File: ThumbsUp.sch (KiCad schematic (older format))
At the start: 169 parts, among them IC1 RP2040, IC2 W25Q128JVSIM, IC3 RP2040, IC4 W25Q128JVSIM, J1 Conn_01x04_Male, J10 Raiser_Male, J11 Raiser_Female, J12 Raiser_Male, J13 Raiser_Female, J14 Raiser_Male, J15 Raiser_Female, J16 Raiser_Male, J17 Raiser_Female, J18 Raiser_Male, J19 Raiser_Female, J2 Conn_01x04_Male, J20 Conn_01x04_Female, J21 Conn_01x04_Female, J22 Conn_01x04_Female, J23 Conn_01x04_Female, J24 Conn_01x04_Male, J25 Conn_01x04_Male, J26 Conn_01x04_Male, J27 Conn_01x04_Male, J28 Conn_01x04_Female, J29 Conn_01x04_Female, J3 Conn_01x04_Female, J30 Conn_01x04_Female, J31 Conn_01x04_Female, J32 USB_C_Receptacle_USB2.0, J33 Raiser_Male, J34 Raiser_Female, J35 Raiser_Male, J36 STX-3501-3N, J37 USB_C_Receptacle_USB2.0, J38 Raiser_Female, J39 Raiser_Male, J4 Conn_01x04_Male, J40 Raiser_Female, J41 Raiser_Male, J42 Raiser_Female, J43 Raiser_Male, J44 Raiser_Female, J45 Raiser_Male, J46 STX-3501-3N, J47 Raiser_Female, J48 Raiser_Male, J49 Raiser_Female, J5 Conn_01x04_Female, J50 Raiser_Male, J51 Raiser_Female, J52 Raiser_Male, J6 Conn_01x04_Male, J7 Conn_01x04_Male, J8 Conn_01x04_Male, J9 Raiser_Female, U1 NCP1117-3.3_SOT223, U2 NCP1117-3.3_SOT223, Y1 ABLS-12.000MHZ-B4-T, Y2 ABLS-12.000MHZ-B4-T

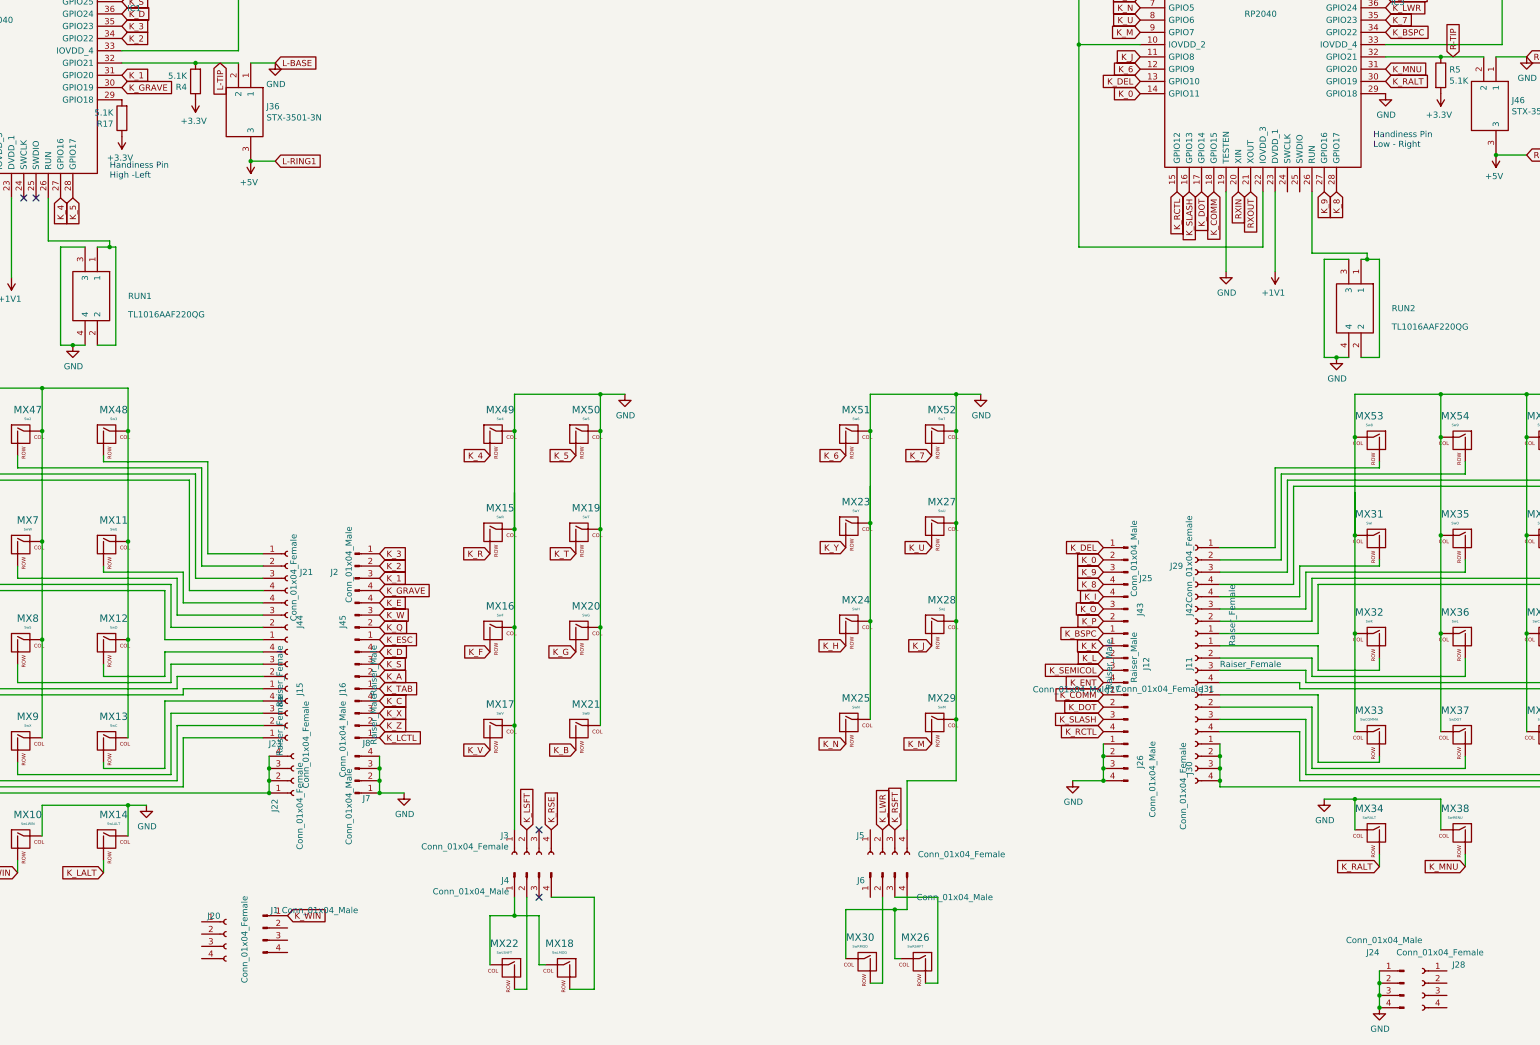
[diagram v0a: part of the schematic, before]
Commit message: Moved the tracks out of L-inner corners
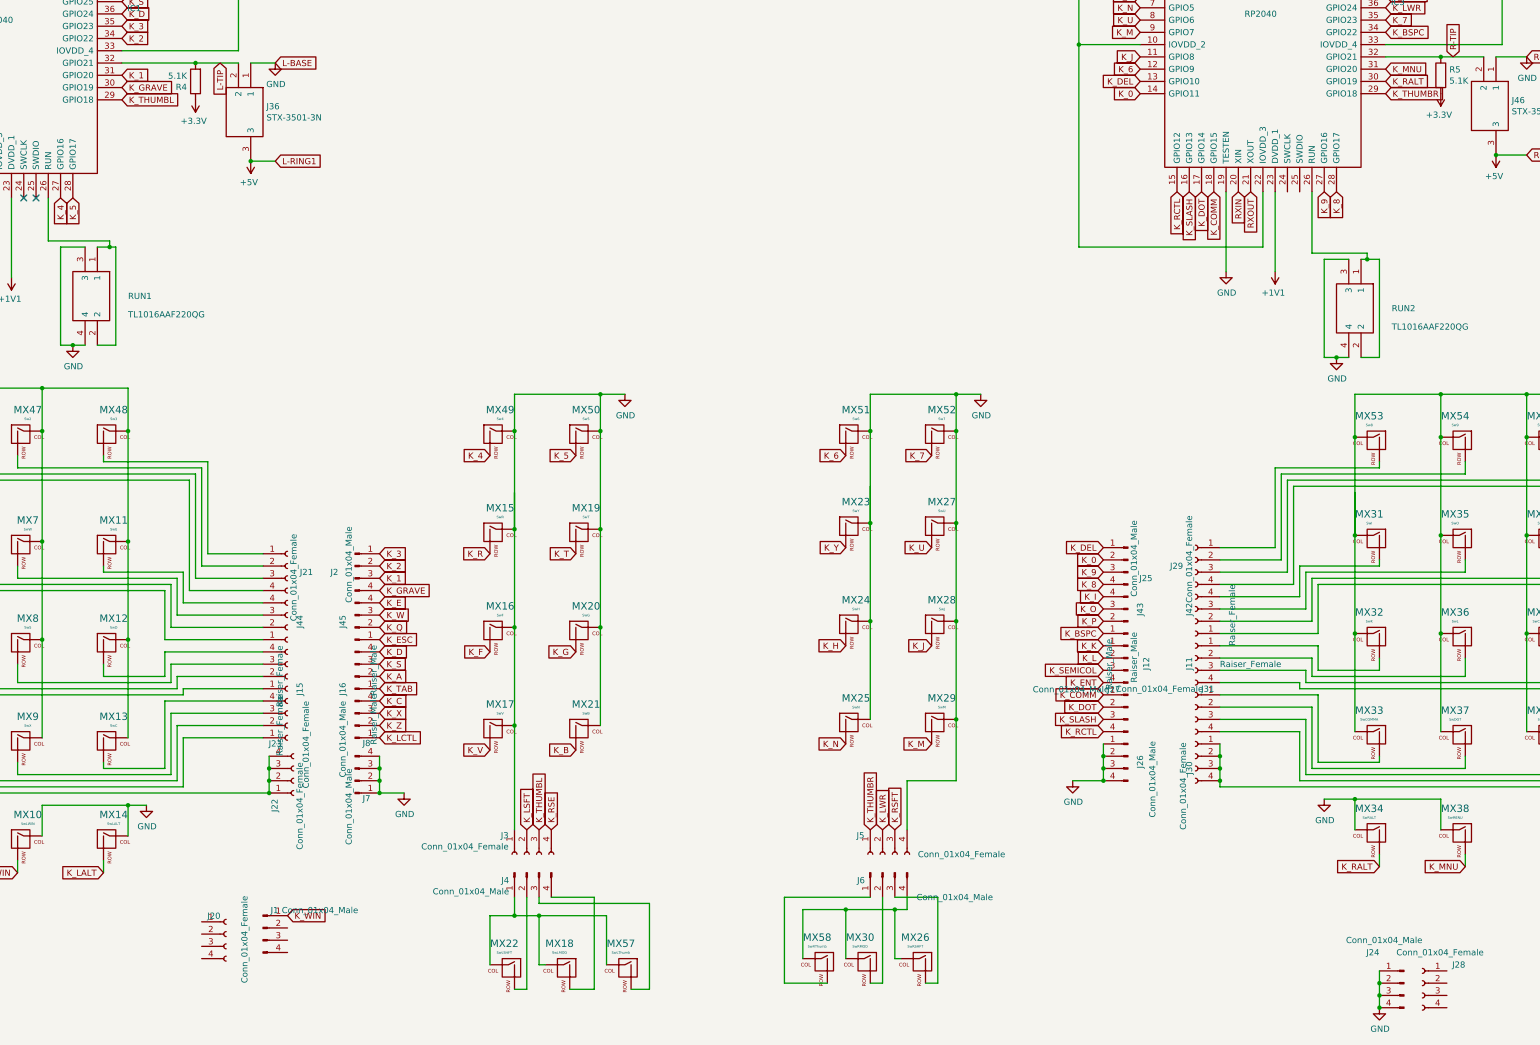
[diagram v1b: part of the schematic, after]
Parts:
- removed R17: 5.1K, Resistor_SMD:R_0402_1005Metric, symbol Device:R
- added MX57: SwLThumb, MX_Alps_Hybrid:MX-1U-NoLED_HotSwap, symbol ThumbsUp-rescue:MX-NoLED-MX_Alps_Hybrid
- added MX58: SwRThumb, MX_Alps_Hybrid:MX-1U-NoLED_HotSwap, symbol ThumbsUp-rescue:MX-NoLED-MX_Alps_Hybrid
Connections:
- net GND: no longer IC3.29 (GPIO18)
- net at J4.1 (Pin_1), MX18.1 (COL), MX22.1 (COL): now also MX57.1 (COL)
- net K_THUMBL: now reaches J3.3 (Pin_3)
- net K_THUMBL: now also IC1.29 (GPIO18)
- net at J4.3 (Pin_3): now also MX57.2 (ROW)
- net at J6.4 (Pin_4), MX26.1 (COL), MX30.1 (COL): now also MX58.1 (COL)
- net K_THUMBR: now reaches J5.1 (Pin_1)
- net K_THUMBR: now also IC3.29 (GPIO18)
- net at J6.1 (Pin_1): now also MX58.2 (ROW)
- no-connect marks 86 -> 84
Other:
- note removed: "Handiness Pin\nHigh -Left"
- note removed: "Handiness Pin\nLow - Right"
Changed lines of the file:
@@
 Wire Wire Line
 	8100 15650 8100 14900
-NoConn ~ 7650 14350
-NoConn ~ 7650 14900
 Wire Wire Line
 	7450 14900 7450 15050
@@
 Text GLabel 2250 7500 0    50   Input ~ 0
 K_C
-$Comp
-L Device:R R17
-U 1 1 63DB25AE
-P 4250 8550
-F 0 "R17" H 4320 8596 50  0000 L CNN
-F 1 "5.1K" H 4320 8505 50  0000 L CNN
-F 2 "Resistor_SMD:R_0402_1005Metric" V 4180 8550 50  0001 C CNN
-F 3 "~" H 4250 8550 50  0001 C CNN
-	1    4250 8550
-	-1   0    0    1
-$EndComp
-$Comp
-L power:+3.3V #PWR0157
-U 1 1 63DB2E0C
-P 4250 8700
-F 0 "#PWR0157" H 4250 8550 50  0001 C CNN
-F 1 "+3.3V" H 4265 8873 50  0000 C CNN
-F 2 "" H 4250 8700 50  0001 C CNN
-F 3 "" H 4250 8700 50  0001 C CNN
-	1    4250 8700
-	-1   0    0    1
-$EndComp
-Text Notes 4150 9050 0    50   ~ 0
-Handiness Pin\nHigh -Left
-Text Notes 14450 8800 0    50   ~ 0
-Handiness Pin\nLow - Right
-$Comp
-L power:GND #PWR0158
-U 1 1 63DB80C5
-P 14550 8350
-F 0 "#PWR0158" H 14550 8100 50  0001 C CNN
-F 1 "GND" H 14555 8177 50  0000 C CNN
-F 2 "" H 14550 8350 50  0001 C CNN
-F 3 "" H 14550 8350 50  0001 C CNN
-	1    14550 8350
-	1    0    0    -1
-$EndComp
 Wire Wire Line
 	6350 13750 6350 13850
@@
 NoConn ~ 18750 10350
 NoConn ~ 18850 10350
+$Comp
+L ThumbsUp-rescue:MX-NoLED-MX_Alps_Hybrid MX57
+U 1 1 645C19C4
+P 8350 15500
+F 0 "MX57" H 8383 15723 60  0000 C CNN
+F 1 "SwLThumb" H 8383 15649 20  0000 C CNN
+F 2 "MX_Alps_Hybrid:MX-1U-NoLED_HotSwap" H 7725 15475 60  0001 C CNN
+F 3 "" H 7725 15475 60  0001 C CNN
+	1    8350 15500
+	-1   0    0    -1
+$EndComp
+Wire Wire Line
+	8200 15450 8200 15050
+Wire Wire Line
+	8200 15050 7650 15050
+Connection ~ 7650 15050
+Wire Wire Line
+	7650 14950 8550 14950
+Wire Wire Line
+	8550 14950 8550 15650
+Wire Wire Line
+	8550 15650 8400 15650
+$Comp
+L ThumbsUp-rescue:MX-NoLED-MX_Alps_Hybrid MX58
+U 1 1 64645FE3
+P 9950 15450
+F 0 "MX58" H 9983 15673 60  0000 C CNN
+F 1 "SwRThumb" H 9983 15599 20  0000 C CNN
+F 2 "MX_Alps_Hybrid:MX-1U-NoLED_HotSwap" H 9325 15425 60  0001 C CNN
+F 3 "" H 9325 15425 60  0001 C CNN
+	1    9950 15450
+	-1   0    0    -1
+$EndComp
+Wire Wire Line
+	10350 14900 9650 14900
+Wire Wire Line
+	9650 14900 9650 15600
+Wire Wire Line
+	9650 15600 10000 15600
+Wire Wire Line
+	9800 15400 9800 15000
+Wire Wire Line
+	9800 15000 10150 15000
+Connection ~ 10150 15000
+Wire Wire Line
+	7650 14900 7650 14950
+Text GLabel 14550 8350 2    50   Input ~ 0
+K_THUMBR
+Text GLabel 4250 8400 2    50   Input ~ 0
+K_THUMBL
+Text GLabel 7650 14350 1    50   Input ~ 0
+K_THUMBL
+Text GLabel 10350 14350 1    50   Input ~ 0
+K_THUMBR
 $EndSCHEMATC
